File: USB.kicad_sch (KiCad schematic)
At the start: 24 parts, among them J10001 USB_OTG, Q10001 Q_PNP_BEC, U3001 rv1126/rv1109

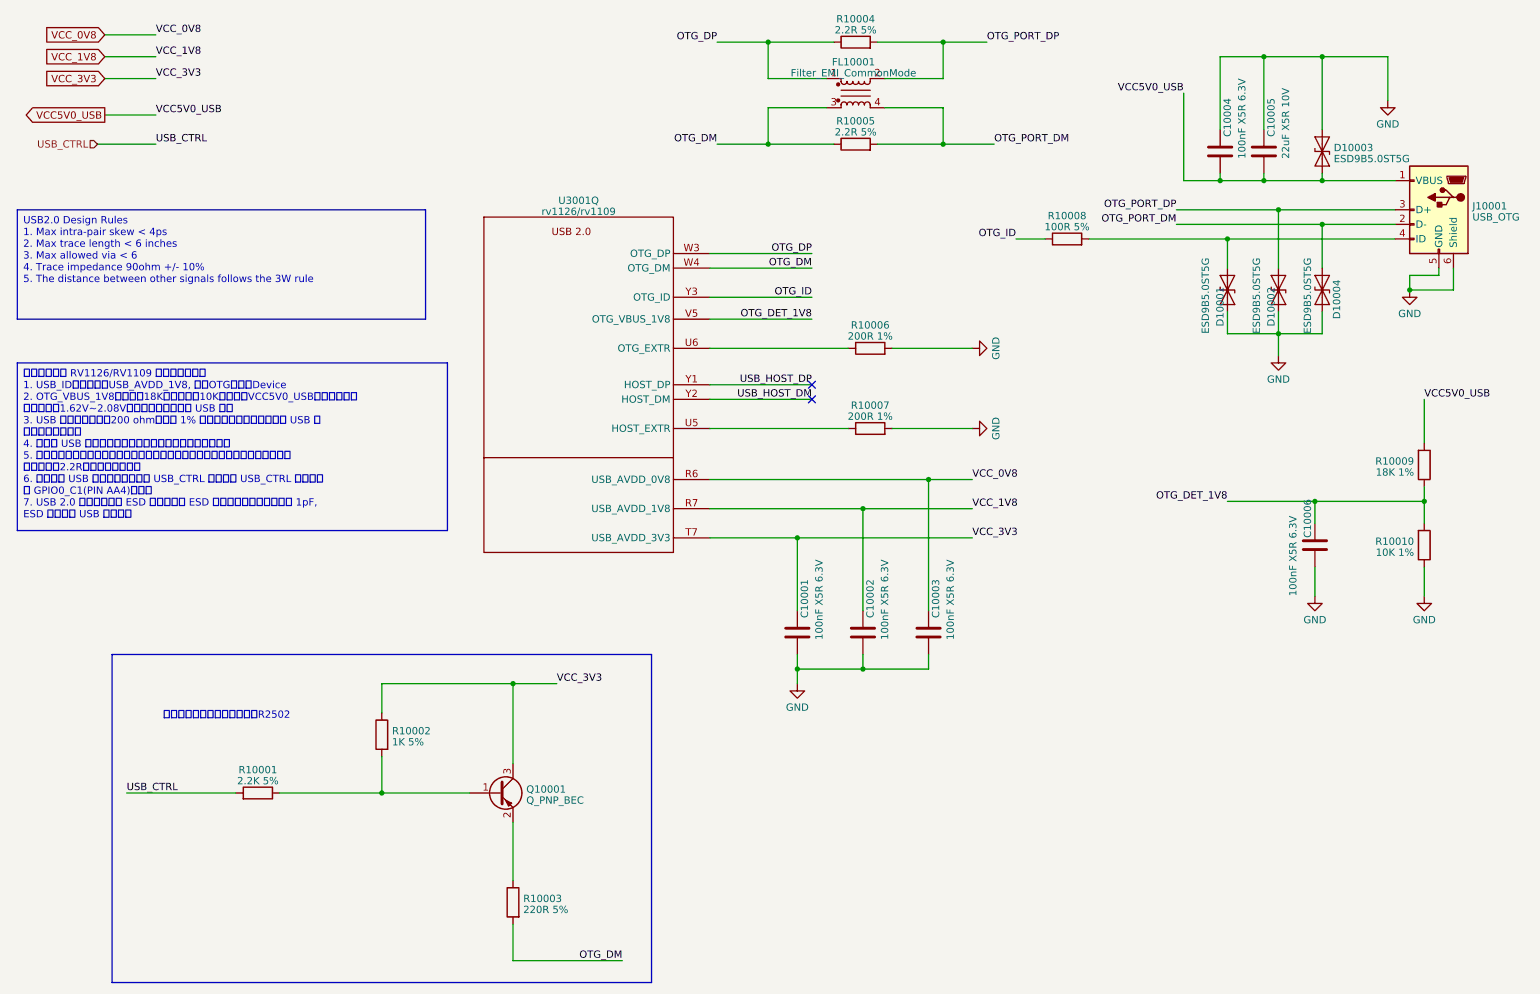
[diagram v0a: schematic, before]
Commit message: move DDR power decoupling capacitors into DDR4 Sheet
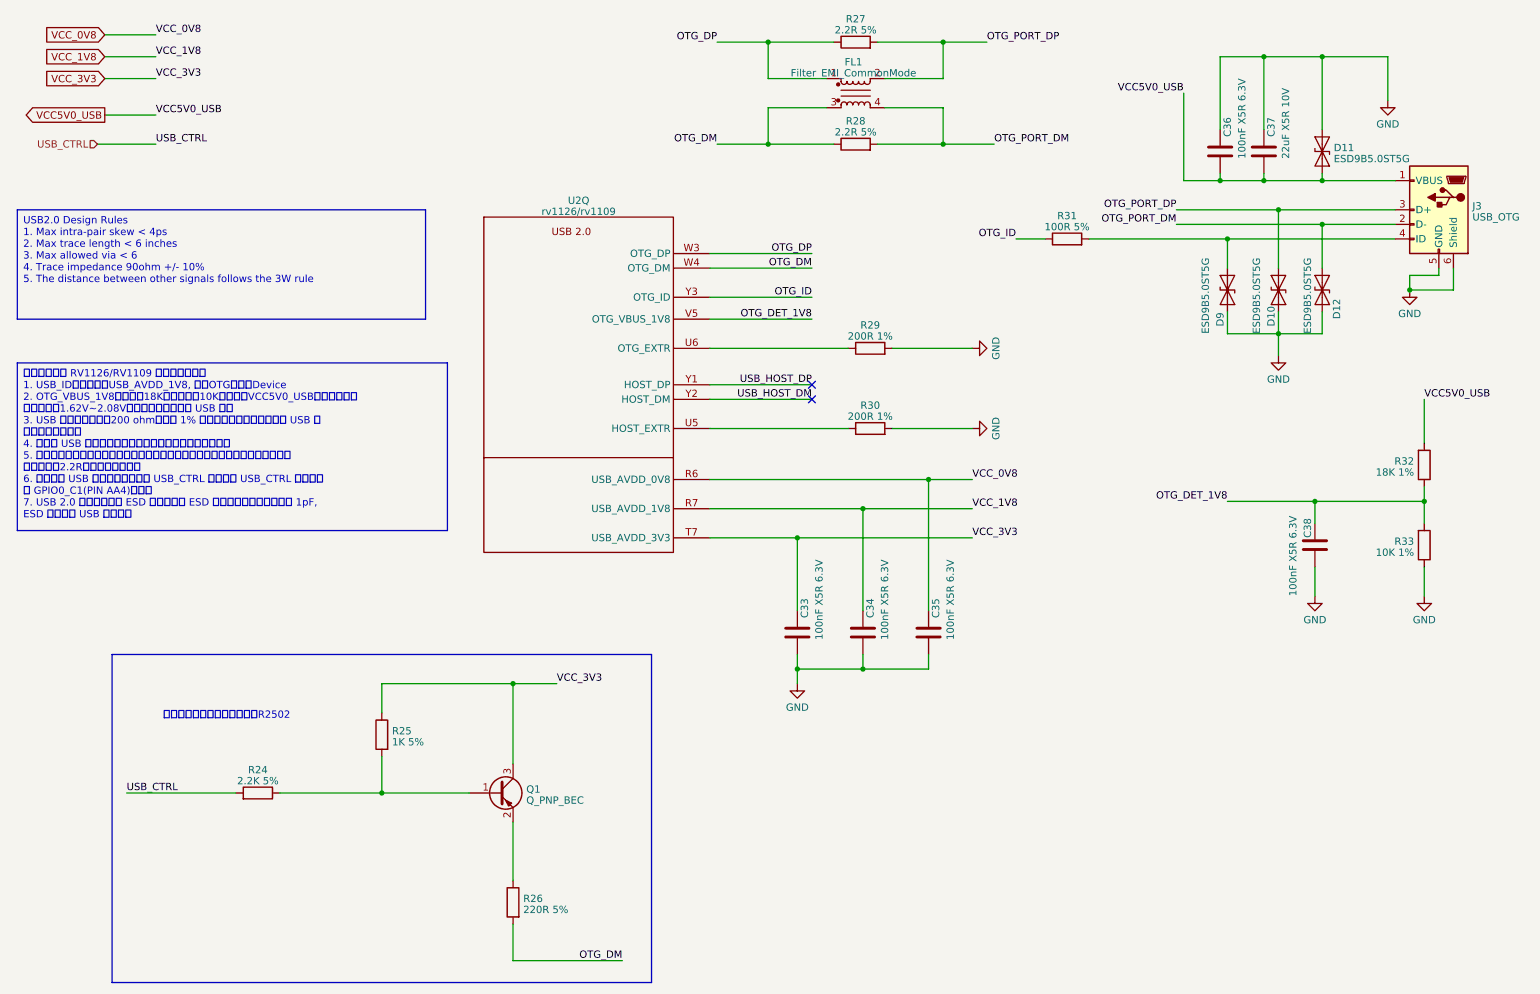
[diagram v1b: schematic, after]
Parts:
- renumbered C10001 to C33, C10002 to C34, C10003 to C35, C10004 to C36, C10005 to C37, C10006 to C38, D10002 to D10, D10003 to D11, D10004 to D12, D10001 to D9, FL10001 to FL1, J10001 to J3, Q10001 to Q1, R10001 to R24, R10002 to R25, R10003 to R26, R10004 to R27, R10005 to R28, R10006 to R29, R10007 to R30, R10008 to R31, R10009 to R32, R10010 to R33, U3001 to U2

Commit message: resort all symbols
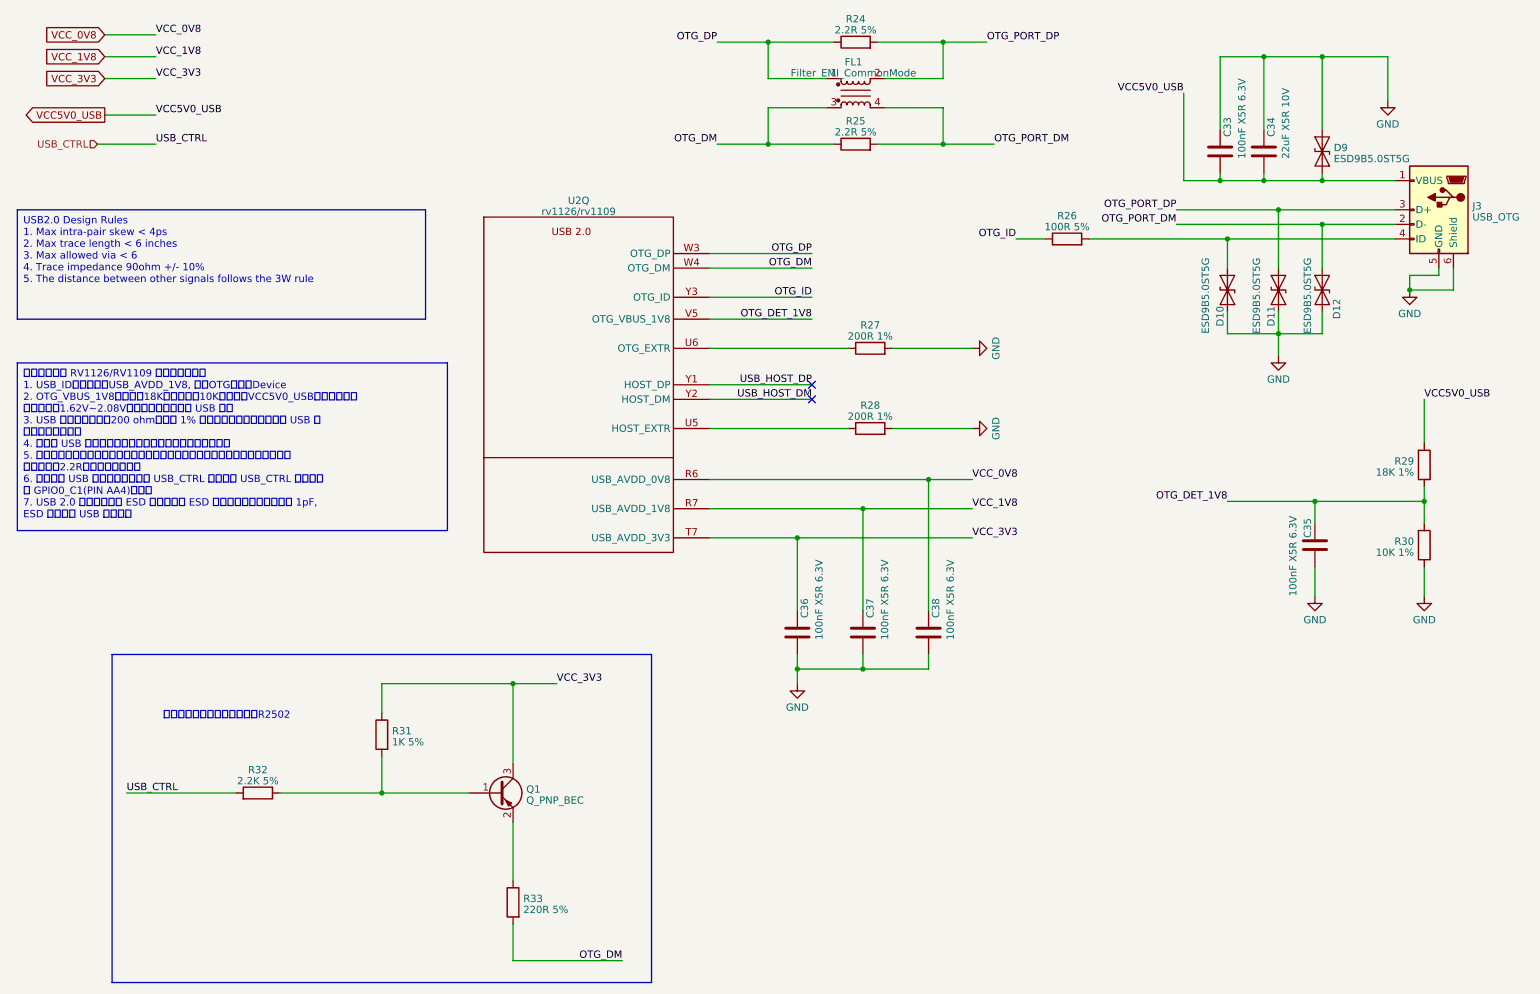
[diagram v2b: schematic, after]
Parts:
- renumbered C36 to C33, C37 to C34, C38 to C35, C33 to C36, C34 to C37, C35 to C38, D9 to D10, D10 to D11, D11 to D9, R27 to R24, R28 to R25, R31 to R26, R29 to R27, R30 to R28, R32 to R29, R33 to R30, R25 to R31, R24 to R32, R26 to R33

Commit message: updated annotations
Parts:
- renumbered R24 to R25, R25 to R26, R26 to R27, R27 to R28, R28 to R29, R29 to R30, R30 to R31, R31 to R32, R32 to R33, R33 to R34
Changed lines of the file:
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@@
   (symbol (lib_id "Device:R") (at 58.42 152.4 270) (mirror x) (unit 1)
     (in_bom yes) (on_board yes) (dnp no) (fields_autoplaced)
-    (property "Reference" "R32" (at 58.42 148.3741 90)
+    (property "Reference" "R33" (at 58.42 148.3741 90)
       (effects (font (size 1.27 1.27)))
     )
@@
       (project "leaf"
         (path "/e3b58043-16a3-43c8-9fad-9c9784eebfa4/be5d8e43-2411-4620-a7a9-8dc1a750f993"
-          (reference "R32") (unit 1)
+          (reference "R33") (unit 1)
         )
       )
@@
   (symbol (lib_id "Device:R") (at 261.62 109.22 0) (mirror x) (unit 1)
     (in_bom yes) (on_board yes) (dnp no) (fields_autoplaced)
-    (property "Reference" "R30" (at 259.842 108.5763 0)
+    (property "Reference" "R31" (at 259.842 108.5763 0)
       (effects (font (size 1.27 1.27)) (justify right))
     )
@@
       (project "leaf"
         (path "/e3b58043-16a3-43c8-9fad-9c9784eebfa4/be5d8e43-2411-4620-a7a9-8dc1a750f993"
-          (reference "R30") (unit 1)
+          (reference "R31") (unit 1)
         )
       )
@@
   (symbol (lib_id "Device:R") (at 165.1 74.93 90) (unit 1)
     (in_bom yes) (on_board yes) (dnp no) (fields_autoplaced)
-    (property "Reference" "R27" (at 165.1 70.9041 90)
+    (property "Reference" "R28" (at 165.1 70.9041 90)
       (effects (font (size 1.27 1.27)))
     )
@@
       (project "leaf"
         (path "/e3b58043-16a3-43c8-9fad-9c9784eebfa4/be5d8e43-2411-4620-a7a9-8dc1a750f993"
-          (reference "R27") (unit 1)
+          (reference "R28") (unit 1)
         )
       )
@@
   (symbol (lib_id "Device:R") (at 199.39 55.88 90) (unit 1)
     (in_bom yes) (on_board yes) (dnp no) (fields_autoplaced)
-    (property "Reference" "R26" (at 199.39 51.8541 90)
+    (property "Reference" "R27" (at 199.39 51.8541 90)
       (effects (font (size 1.27 1.27)))
     )
@@
       (project "leaf"
         (path "/e3b58043-16a3-43c8-9fad-9c9784eebfa4/be5d8e43-2411-4620-a7a9-8dc1a750f993"
+          (reference "R27") (unit 1)
+        )
+      )
+    )
+  )
+  (symbol (lib_id "Device:R") (at 102.87 171.45 0) (mirror y) (unit 1)
+    (in_bom yes) (on_board yes) (dnp no) (fields_autoplaced)
+    (property "Reference" "R34" (at 104.648 170.8063 0)
+      (effects (font (size 1.27 1.27)) (justify right))
+    )
+    (property "Value" "220R 5%" (at 104.648 172.7273 0)
+      (effects (font (size 1.27 1.27)) (justify right))
+    )
+    (property "Footprint" "Resistor_SMD:R_0402_1005Metric" (at 104.648 171.45 90)
+      (effects (font (size 1.27 1.27)) hide)
+    )
+    (property "Datasheet" "~" (at 102.87 171.45 0)
+      (effects (font (size 1.27 1.27)) hide)
+    )
+    (pin "1")
+    (pin "2")
+    (instances
+      (project "leaf"
+        (path "/e3b58043-16a3-43c8-9fad-9c9784eebfa4/be5d8e43-2411-4620-a7a9-8dc1a750f993"
+          (reference "R34") (unit 1)
+        )
+      )
+    )
+  )
+  (symbol (lib_id "Device:R") (at 162.56 39.37 90) (unit 1)
+    (in_bom yes) (on_board yes) (dnp no) (fields_autoplaced)
+    (property "Reference" "R26" (at 162.56 35.3441 90)
+      (effects (font (size 1.27 1.27)))
+    )
+    (property "Value" "2.2R 5%" (at 162.56 37.2651 90)
+      (effects (font (size 1.27 1.27)))
+    )
+    (property "Footprint" "Resistor_SMD:R_0603_1608Metric" (at 162.56 41.148 90)
+      (effects (font (size 1.27 1.27)) hide)
+    )
+    (property "Datasheet" "~" (at 162.56 39.37 0)
+      (effects (font (size 1.27 1.27)) hide)
+    )
+    (pin "1")
+    (pin "2")
+    (instances
+      (project "leaf"
+        (path "/e3b58043-16a3-43c8-9fad-9c9784eebfa4/be5d8e43-2411-4620-a7a9-8dc1a750f993"
           (reference "R26") (unit 1)
         )
@@
     )
   )
-  (symbol (lib_id "Device:R") (at 102.87 171.45 0) (mirror y) (unit 1)
-    (in_bom yes) (on_board yes) (dnp no) (fields_autoplaced)
-    (property "Reference" "R33" (at 104.648 170.8063 0)
-      (effects (font (size 1.27 1.27)) (justify right))
-    )
-    (property "Value" "220R 5%" (at 104.648 172.7273 0)
-      (effects (font (size 1.27 1.27)) (justify right))
-    )
-    (property "Footprint" "Resistor_SMD:R_0402_1005Metric" (at 104.648 171.45 90)
-      (effects (font (size 1.27 1.27)) hide)
-    )
-    (property "Datasheet" "~" (at 102.87 171.45 0)
-      (effects (font (size 1.27 1.27)) hide)
-    )
-    (pin "1")
-    (pin "2")
-    (instances
-      (project "leaf"
-        (path "/e3b58043-16a3-43c8-9fad-9c9784eebfa4/be5d8e43-2411-4620-a7a9-8dc1a750f993"
-          (reference "R33") (unit 1)
-        )
-      )
-    )
-  )
-  (symbol (lib_id "Device:R") (at 162.56 39.37 90) (unit 1)
-    (in_bom yes) (on_board yes) (dnp no) (fields_autoplaced)
-    (property "Reference" "R25" (at 162.56 35.3441 90)
-      (effects (font (size 1.27 1.27)))
-    )
-    (property "Value" "2.2R 5%" (at 162.56 37.2651 90)
-      (effects (font (size 1.27 1.27)))
-    )
-    (property "Footprint" "Resistor_SMD:R_0603_1608Metric" (at 162.56 41.148 90)
-      (effects (font (size 1.27 1.27)) hide)
-    )
-    (property "Datasheet" "~" (at 162.56 39.37 0)
-      (effects (font (size 1.27 1.27)) hide)
-    )
-    (pin "1")
-    (pin "2")
-    (instances
-      (project "leaf"
-        (path "/e3b58043-16a3-43c8-9fad-9c9784eebfa4/be5d8e43-2411-4620-a7a9-8dc1a750f993"
-          (reference "R25") (unit 1)
-        )
-      )
-    )
-  )
   (symbol (lib_id "Device:R") (at 261.62 95.25 0) (mirror x) (unit 1)
     (in_bom yes) (on_board yes) (dnp no) (fields_autoplaced)
-    (property "Reference" "R29" (at 259.842 94.6063 0)
+    (property "Reference" "R30" (at 259.842 94.6063 0)
       (effects (font (size 1.27 1.27)) (justify right))
     )
@@
       (project "leaf"
         (path "/e3b58043-16a3-43c8-9fad-9c9784eebfa4/be5d8e43-2411-4620-a7a9-8dc1a750f993"
-          (reference "R29") (unit 1)
+          (reference "R30") (unit 1)
         )
       )
@@
   (symbol (lib_id "Device:R") (at 165.1 88.9 90) (unit 1)
     (in_bom yes) (on_board yes) (dnp no) (fields_autoplaced)
-    (property "Reference" "R28" (at 165.1 84.8741 90)
+    (property "Reference" "R29" (at 165.1 84.8741 90)
       (effects (font (size 1.27 1.27)))
     )
@@
       (project "leaf"
         (path "/e3b58043-16a3-43c8-9fad-9c9784eebfa4/be5d8e43-2411-4620-a7a9-8dc1a750f993"
-          (reference "R28") (unit 1)
+          (reference "R29") (unit 1)
         )
       )
@@
   (symbol (lib_id "Device:R") (at 80.01 142.24 0) (mirror y) (unit 1)
     (in_bom yes) (on_board yes) (dnp no) (fields_autoplaced)
-    (property "Reference" "R31" (at 81.788 141.5963 0)
+    (property "Reference" "R32" (at 81.788 141.5963 0)
       (effects (font (size 1.27 1.27)) (justify right))
     )
@@
       (project "leaf"
         (path "/e3b58043-16a3-43c8-9fad-9c9784eebfa4/be5d8e43-2411-4620-a7a9-8dc1a750f993"
-          (reference "R31") (unit 1)
+          (reference "R32") (unit 1)
         )
       )
@@
   (symbol (lib_id "Device:R") (at 162.56 21.59 90) (unit 1)
     (in_bom yes) (on_board yes) (dnp no) (fields_autoplaced)
-    (property "Reference" "R24" (at 162.56 17.5641 90)
+    (property "Reference" "R25" (at 162.56 17.5641 90)
       (effects (font (size 1.27 1.27)))
     )
@@
       (project "leaf"
         (path "/e3b58043-16a3-43c8-9fad-9c9784eebfa4/be5d8e43-2411-4620-a7a9-8dc1a750f993"
-          (reference "R24") (unit 1)
-        )
-      )
+          (reference "R25") (unit 1)
+        )
+      )

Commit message: added README and license
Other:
- company: Qingdao IotPi Information Technology -> Yang Hongbo
- title: Leaf RV1126 RK809 USB OTG -> Leaf RV1126
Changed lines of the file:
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@@
   (paper "A4")
   (title_block
-    (title "Leaf RV1126 RK809 USB OTG")
-    (date "2023-02-25")
+    (title "Leaf RV1126")
+    (date "2023-06-07")
     (rev "1")
-    (company "Qingdao IotPi Information Technology")
+    (company "Yang Hongbo")
+    (comment 1 "License: CC BY-SA")
   )
   (junction (at 243.84 24.13) (diameter 0) (color 0 0 0 0)

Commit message: fix Q1
was flipped
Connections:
- net VCC_3V3: now also Q1.2 (E); no longer Q1.3 (C)
- net at R34.1: now also Q1.3 (C); no longer Q1.2 (E)
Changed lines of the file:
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@@
     )
   )
-  (symbol (lib_id "Device:Q_PNP_BEC") (at 100.33 152.4 0) (unit 1)
-    (in_bom yes) (on_board yes) (dnp no) (fields_autoplaced)
-    (property "Reference" "Q1" (at 105.1814 151.7563 0)
+  (symbol (lib_id "Device:Q_PNP_BEC") (at 100.33 152.4 0) (mirror x) (unit 1)
+    (in_bom yes) (on_board yes) (dnp no)
+    (property "Reference" "Q1" (at 105.1814 153.0437 0)
       (effects (font (size 1.27 1.27)) (justify left))
     )
-    (property "Value" "Q_PNP_BEC" (at 105.1814 153.6773 0)
+    (property "Value" "Q_PNP_BEC" (at 105.1814 151.1227 0)
       (effects (font (size 1.27 1.27)) (justify left))
     )
-    (property "Footprint" "Package_TO_SOT_SMD:SOT-23" (at 105.41 149.86 0)
+    (property "Footprint" "Package_TO_SOT_SMD:SOT-23" (at 105.41 154.94 0)
       (effects (font (size 1.27 1.27)) hide)
     )

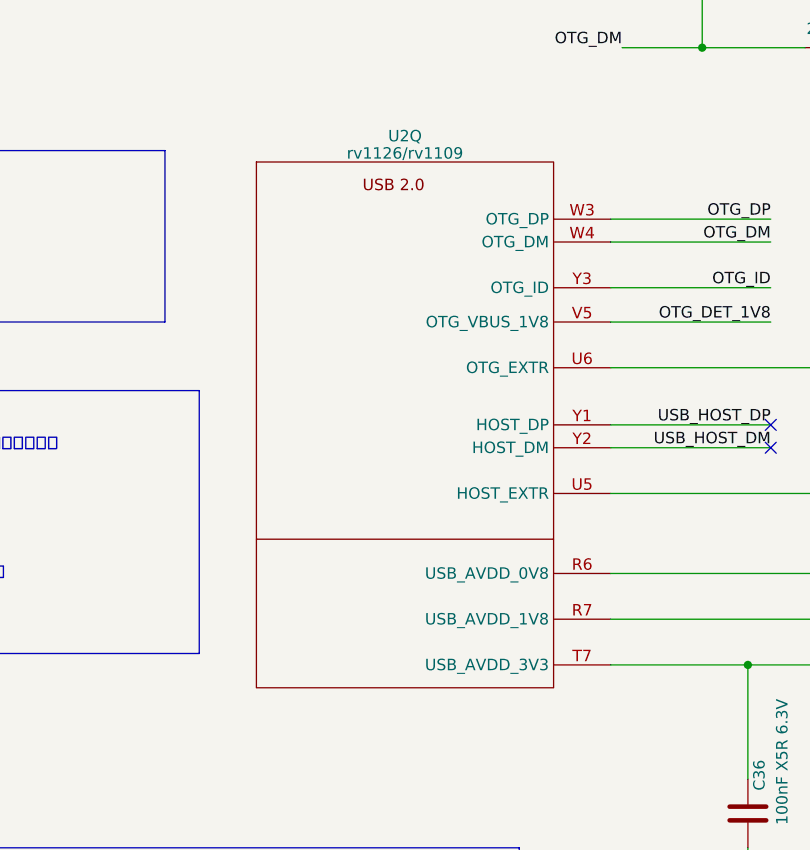
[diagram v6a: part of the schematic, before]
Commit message: replaced Leaf specified symbols with unified iotpi symbols
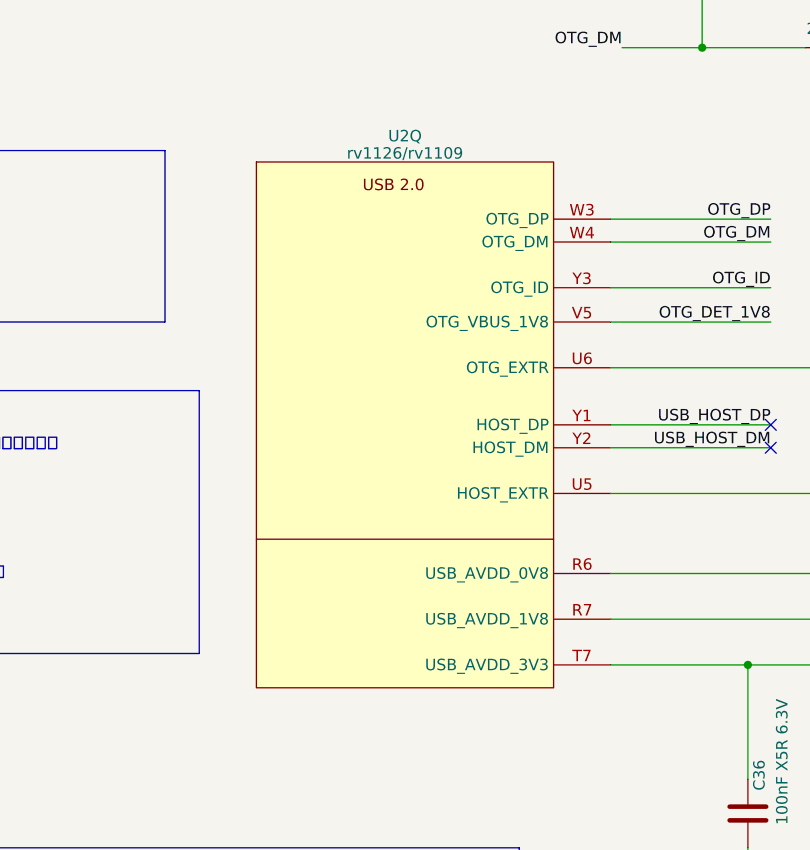
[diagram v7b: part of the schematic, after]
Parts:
- U2: symbol CPU_Rockchip:rv1126_rv1109 -> IotPi_CPU_Rockchip:rv1126_rv1109
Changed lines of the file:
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@@
     )
   )
-  (symbol (lib_id "CPU_Rockchip:rv1126_rv1109") (at 114.3 77.47 0) (unit 17)
+  (symbol (lib_id "IotPi_CPU_Rockchip:rv1126_rv1109") (at 114.3 77.47 0) (unit 17)
     (in_bom yes) (on_board yes) (dnp no) (fields_autoplaced)
     (property "Reference" "U2" (at 114.3 49.1871 0)
@@
       (effects (font (size 1.27 1.27)))
     )
-    (property "Footprint" "Rockchip_SoC:Rockchip_RV1126_FCCSP409LD_14.0x14.0mm" (at 140.97 104.14 0)
+    (property "Footprint" "Rockchip_SoC:Rockchip_RV1126_FCCSP409LD_14.0x14.0mm" (at 146.05 124.46 0)
       (effects (font (size 1.27 1.27)) hide)
     )
-    (property "Datasheet" "" (at 140.97 104.14 0)
+    (property "Datasheet" "" (at 146.05 124.46 0)
       (effects (font (size 1.27 1.27)) hide)
     )

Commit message: replaced Leaf libraries with combined libraries
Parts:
- U2: footprint Rockchip_SoC:Rockchip_RV1126_FCCSP409LD_14.0x14.0mm -> IotPi_Rockchip_SoC:Rockchip_RV1126_FCCSP409LD_14.0x14.0mm
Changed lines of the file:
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@@
       (effects (font (size 1.27 1.27)))
     )
-    (property "Footprint" "Rockchip_SoC:Rockchip_RV1126_FCCSP409LD_14.0x14.0mm" (at 146.05 124.46 0)
+    (property "Footprint" "IotPi_Rockchip_SoC:Rockchip_RV1126_FCCSP409LD_14.0x14.0mm" (at 146.05 124.46 0)
       (effects (font (size 1.27 1.27)) hide)
     )
